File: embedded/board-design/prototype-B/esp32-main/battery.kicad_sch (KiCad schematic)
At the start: 15 parts, among them J7 Conn_01x02_Socket, J8 Conn_01x03_Socket, Q5 FDN340P, Q6 FDN340P, U5 LTC4054ES5-4.2

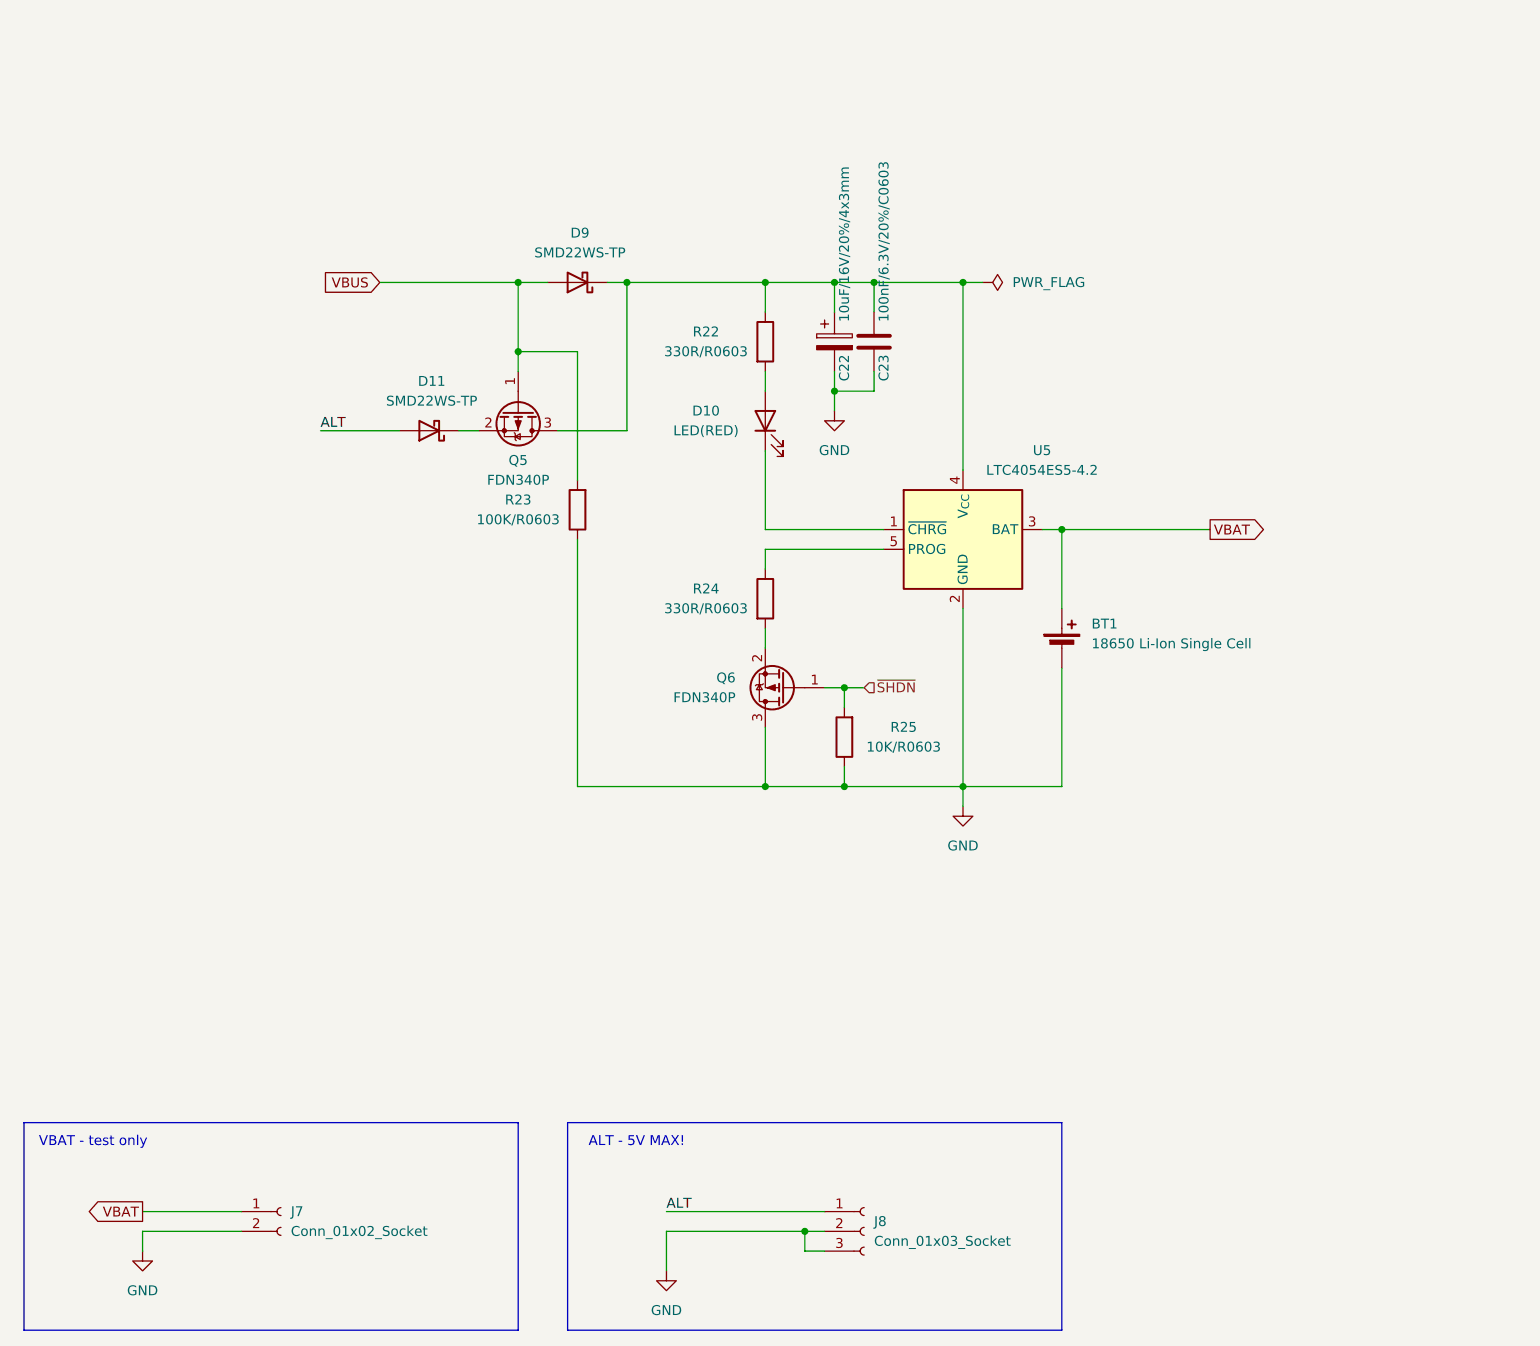
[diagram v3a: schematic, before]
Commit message: [prototype-B]
Refactored power scheme. Updated prototype-B README.md.

Signed-off-by: Nicolae-Andrei Vasile <vasilenicolaeandrei@gmail.com>
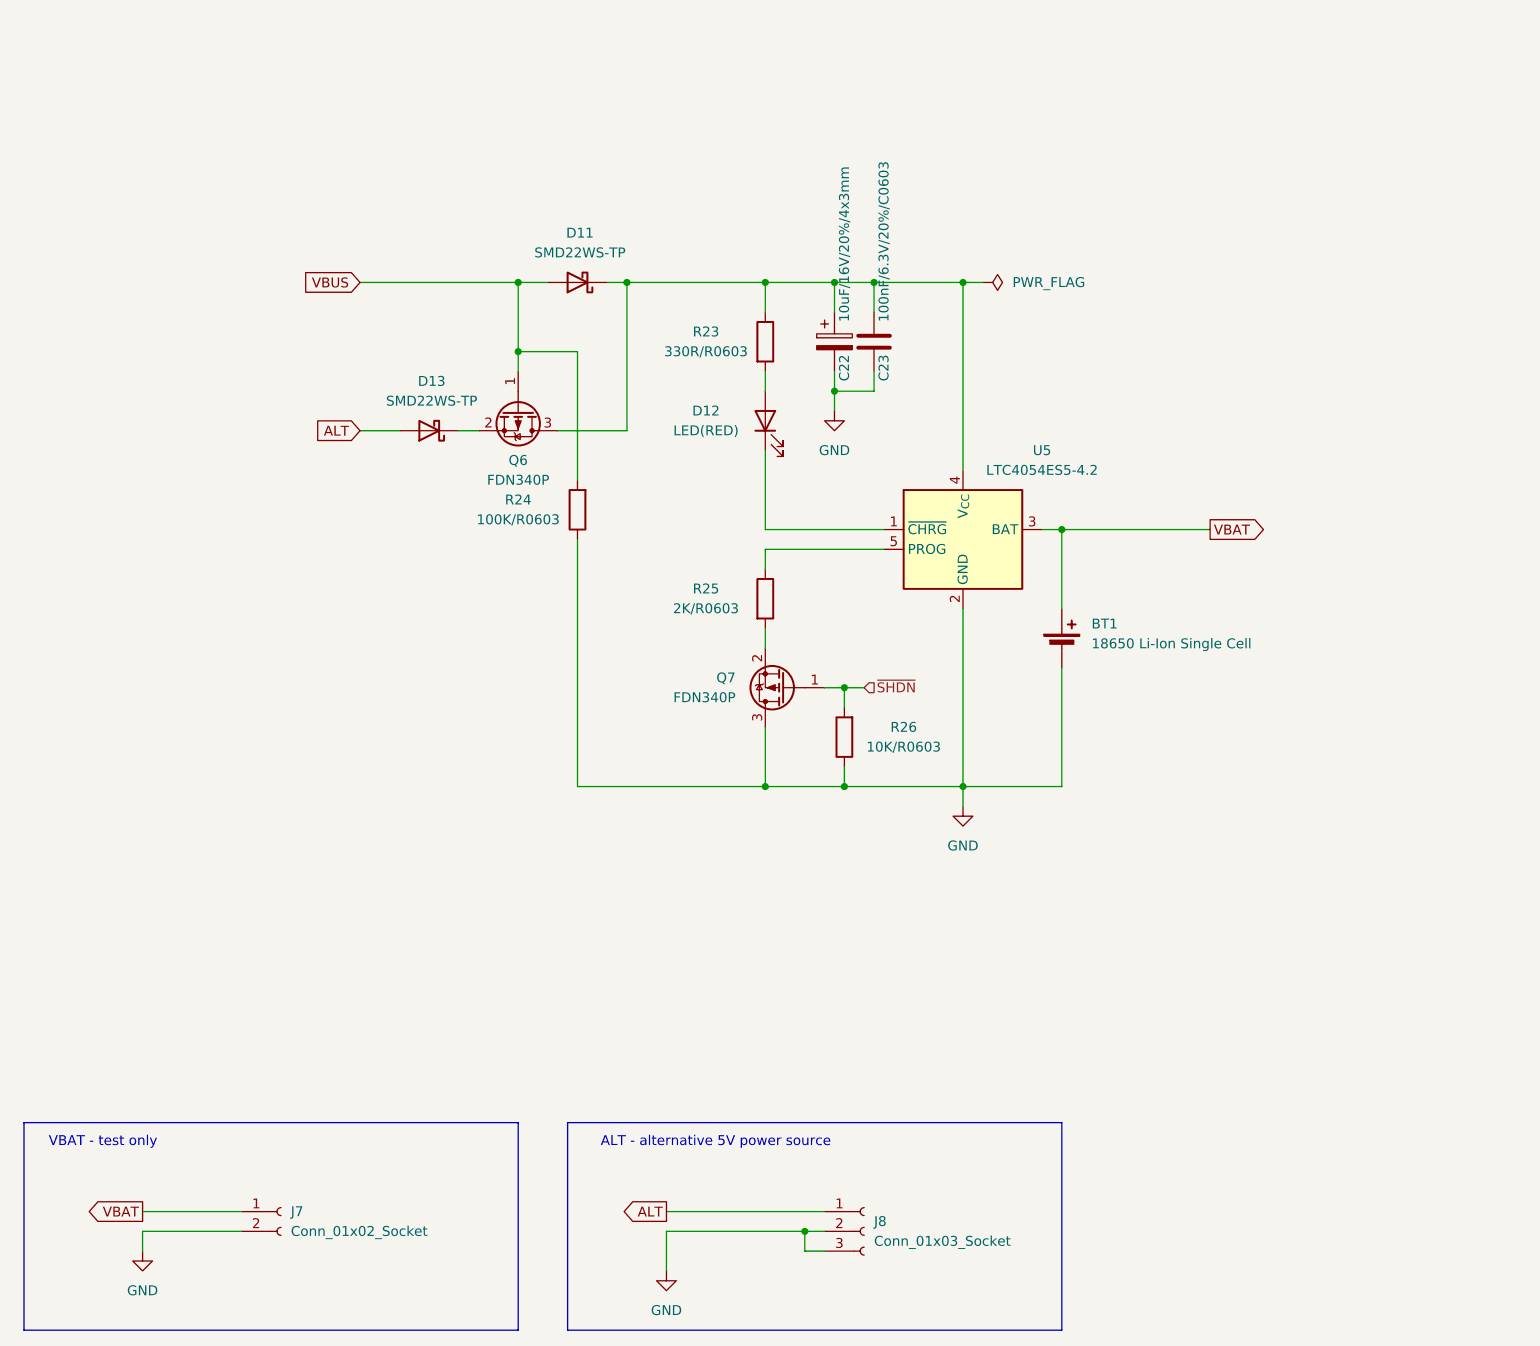
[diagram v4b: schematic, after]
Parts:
- R25: renamed from R24; value 330R/R0603 -> 2K/R0603
- renumbered D9 to D11, D10 to D12, D11 to D13, Q5 to Q6, Q6 to Q7, R22 to R23, R23 to R24, R25 to R26
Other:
- note added: "ALT - alternative 5V power source"
- note removed: "ALT - 5V MAX!"
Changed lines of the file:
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@@
 	(wire
 		(pts
-			(xy 83.82 58.42) (xy 101.6 58.42)
+			(xy 81.28 58.42) (xy 101.6 58.42)
 		)
 		(stroke
@@
 	(wire
 		(pts
-			(xy 76.2 77.47) (xy 86.36 77.47)
+			(xy 81.28 77.47) (xy 86.36 77.47)
 		)
 		(stroke
@@
 	(text "VBAT - test only"
 		(exclude_from_sim no)
-		(at 46.99 168.91 0)
+		(at 48.26 168.91 0)
 		(effects
 			(font
@@
 		)
 	)
-	(text "ALT - 5V MAX!"
+	(text "ALT - alternative 5V power source"
 		(exclude_from_sim no)
-		(at 116.84 168.91 0)
+		(at 127 168.91 0)
 		(effects
 			(font
@@
 		)
 	)
-	(label "ALT"
-		(at 120.65 177.8 0)
+	(global_label "VBUS"
+		(shape input)
+		(at 81.28 58.42 180)
 		(fields_autoplaced yes)
 		(effects
@@
 				(size 1.27 1.27)
 			)
-			(justify left bottom)
-		)
-	)
-	(label "ALT"
-		(at 76.2 77.47 0)
+			(justify right)
+		)
+		(property "Intersheetrefs" "${INTERSHEET_REFS}"
+			(at 73.3962 58.42 0)
+			(effects
+				(font
+					(size 1.27 1.27)
+				)
+				(justify right)
+				(hide yes)
+			)
+		)
+	)
+	(global_label "ALT"
+		(shape output)
+		(at 120.65 177.8 180)
 		(fields_autoplaced yes)
 		(effects
@@
 				(size 1.27 1.27)
 			)
-			(justify left bottom)
-		)
-	)
-	(global_label "VBUS"
-		(shape input)
-		(at 83.82 58.42 180)
-		(fields_autoplaced yes)
-		(effects
-			(font
-				(size 1.27 1.27)
-			)
 			(justify right)
 		)
 		(property "Intersheetrefs" "${INTERSHEET_REFS}"
-			(at 75.9362 58.42 0)
+			(at 114.5805 177.8 0)
 			(effects
 				(font
@@
 				)
 				(justify left)
+				(hide yes)
+			)
+		)
+	)
+	(global_label "ALT"
+		(shape input)
+		(at 81.28 77.47 180)
+		(fields_autoplaced yes)
+		(effects
+			(font
+				(size 1.27 1.27)
+			)
+			(justify right)
+		)
+		(property "Intersheetrefs" "${INTERSHEET_REFS}"
+			(at 75.2105 77.47 0)
+			(effects
+				(font
+					(size 1.27 1.27)
+				)
+				(justify right)
 				(hide yes)
 			)
@@
 		(on_board yes)
 		(dnp no)
-		(property "Reference" "D9"
+		(property "Reference" "D11"
 			(at 109.5375 52.07 0)
 			(effects
@@
 			(project "esp32-main"
 				(path "/6d02e045-d1b3-4320-a4f8-f5e2c734acd4/9cfdfa29-fef4-49c3-96a5-094ec94d9453"
-					(reference "D9")
+					(reference "D11")
 					(unit 1)
 				)
@@
 		(on_board yes)
 		(dnp no)
-		(property "Reference" "R22"
+		(property "Reference" "R23"
 			(at 125.73 64.77 0)
 			(effects
@@
 			(project "esp32-main"
 				(path "/6d02e045-d1b3-4320-a4f8-f5e2c734acd4/9cfdfa29-fef4-49c3-96a5-094ec94d9453"
-					(reference "R22")
+					(reference "R23")
 					(unit 1)
 				)
@@
 		(on_board yes)
 		(dnp no)
-		(property "Reference" "R23"
+		(property "Reference" "R24"
 			(at 101.6 86.36 0)
 			(effects
@@
 			(project "esp32-main"
 				(path "/6d02e045-d1b3-4320-a4f8-f5e2c734acd4/9cfdfa29-fef4-49c3-96a5-094ec94d9453"
-					(reference "R23")
+					(reference "R24")
 					(unit 1)
 				)
@@
 		(dnp no)
 		(fields_autoplaced yes)
-		(property "Reference" "Q5"
+		(property "Reference" "Q6"
 			(at 101.6 81.28 90)
 			(effects
@@
 			(project "esp32-main"
 				(path "/6d02e045-d1b3-4320-a4f8-f5e2c734acd4/9cfdfa29-fef4-49c3-96a5-094ec94d9453"
-					(reference "Q5")
+					(reference "Q6")
 					(unit 1)
 				)
@@
 		(dnp no)
 		(fields_autoplaced yes)
-		(property "Reference" "#PWR026"
+		(property "Reference" "#PWR023"
 			(at 158.75 132.08 0)
 			(effects
@@
 			(project "esp32-main"
 				(path "/6d02e045-d1b3-4320-a4f8-f5e2c734acd4/9cfdfa29-fef4-49c3-96a5-094ec94d9453"
-					(reference "#PWR026")
+					(reference "#PWR023")
 					(unit 1)
 				)
@@
 		(dnp no)
 		(fields_autoplaced yes)
-		(property "Reference" "Q6"
+		(property "Reference" "Q7"
 			(at 129.54 109.2199 0)
 			(effects
@@
 			(project "esp32-main"
 				(path "/6d02e045-d1b3-4320-a4f8-f5e2c734acd4/9cfdfa29-fef4-49c3-96a5-094ec94d9453"
-					(reference "Q6")
+					(reference "Q7")
 					(unit 1)
 				)
@@
 		(dnp no)
 		(fields_autoplaced yes)
-		(property "Reference" "#PWR027"
+		(property "Reference" "#PWR025"
 			(at 120.65 191.77 0)
 			(effects
@@
 			(project "esp32-main"
 				(path "/6d02e045-d1b3-4320-a4f8-f5e2c734acd4/9cfdfa29-fef4-49c3-96a5-094ec94d9453"
-					(reference "#PWR027")
+					(reference "#PWR025")
 					(unit 1)
 				)
@@
 		(on_board yes)
 		(dnp no)
-		(property "Reference" "D11"
+		(property "Reference" "D13"
 			(at 90.4875 71.12 0)
 			(effects
@@
 			(project "esp32-main"
 				(path "/6d02e045-d1b3-4320-a4f8-f5e2c734acd4/9cfdfa29-fef4-49c3-96a5-094ec94d9453"
-					(reference "D11")
+					(reference "D13")
 					(unit 1)
 				)
@@
 		(dnp no)
 		(fields_autoplaced yes)
-		(property "Reference" "#PWR023"
+		(property "Reference" "#PWR024"
 			(at 53.34 189.23 0)
 			(effects
@@
 			(project "esp32-main"
 				(path "/6d02e045-d1b3-4320-a4f8-f5e2c734acd4/9cfdfa29-fef4-49c3-96a5-094ec94d9453"
-					(reference "#PWR023")
+					(reference "#PWR024")
 					(unit 1)
 				)
@@
 		(dnp no)
 		(fields_autoplaced yes)
-		(property "Reference" "#PWR025"
+		(property "Reference" "#PWR022"
 			(at 142.24 81.28 0)
 			(effects
@@
 			(project "esp32-main"
 				(path "/6d02e045-d1b3-4320-a4f8-f5e2c734acd4/9cfdfa29-fef4-49c3-96a5-094ec94d9453"
-					(reference "#PWR025")
+					(reference "#PWR022")
 					(unit 1)
 				)
@@
 		(on_board yes)
 		(dnp no)
-		(property "Reference" "R25"
+		(property "Reference" "R26"
 			(at 151.13 115.57 0)
 			(effects
@@
 			(project "esp32-main"
 				(path "/6d02e045-d1b3-4320-a4f8-f5e2c734acd4/9cfdfa29-fef4-49c3-96a5-094ec94d9453"
-					(reference "R25")
+					(reference "R26")
 					(unit 1)
 				)
@@
 		(on_board yes)
 		(dnp no)
-		(property "Reference" "R24"
+		(property "Reference" "R25"
 			(at 125.73 97.79 0)
 			(effects
@@
 			)
 		)
-		(property "Value" "330R/R0603"
+		(property "Value" "2K/R0603"
 			(at 125.73 100.33 0)
 			(effects
@@
 			(project "esp32-main"
 				(path "/6d02e045-d1b3-4320-a4f8-f5e2c734acd4/9cfdfa29-fef4-49c3-96a5-094ec94d9453"
-					(reference "R24")
+					(reference "R25")
 					(unit 1)
 				)
@@
 		(on_board yes)
 		(dnp no)
-		(property "Reference" "D10"
+		(property "Reference" "D12"
 			(at 125.73 74.93 90)
 			(effects
@@
 			(project "esp32-main"
 				(path "/6d02e045-d1b3-4320-a4f8-f5e2c734acd4/9cfdfa29-fef4-49c3-96a5-094ec94d9453"
-					(reference "D10")
+					(reference "D12")
 					(unit 1)
 				)

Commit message: [prototype-B]
Refactored hardware implementation.

Signed-off-by: Nicolae-Andrei Vasile <vasilenicolaeandrei@gmail.com>
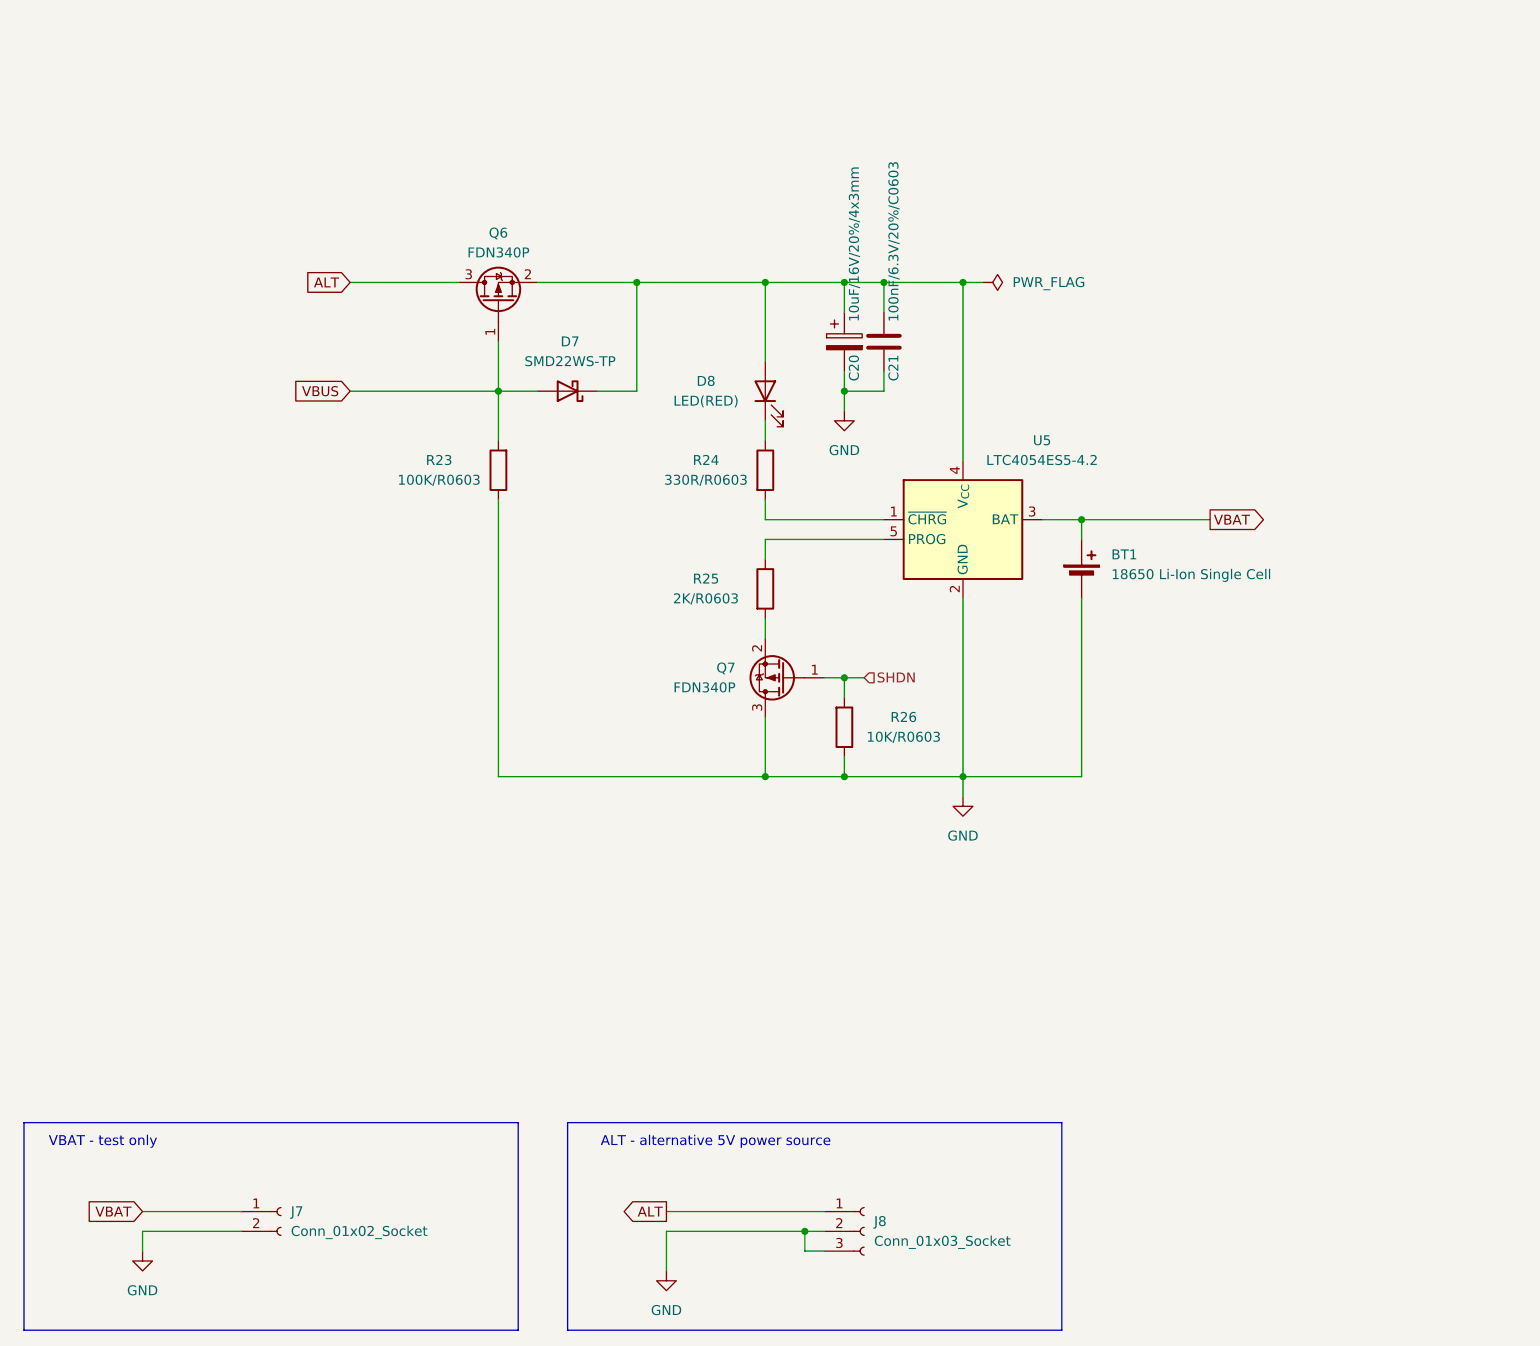
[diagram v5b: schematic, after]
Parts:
- removed D13: SMD22WS-TP, Diode_SMD:D_SOD-323_HandSoldering, symbol Device:D_Schottky
- renumbered C22 to C20, C23 to C21, D11 to D7, D12 to D8, R24 to R23, R23 to R24
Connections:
- net ALT: now also Q6.3 (D)
- net at C20.1, C21.1, D7.1 (K)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: now also D8.2 (A), Q6.2 (S); no longer Q6.3 (D), R24.1
- net at R24.2: now also U5.1 (~{CHRG}); no longer D8.2 (A)
- net at D8.1 (K): now also R24.1; no longer U5.1 (~{CHRG})
- net ~{SHDN} renamed SHDN
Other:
- moved on the sheet: BT1, C20, C21, D7, D8, R23, R24, R25, U5
